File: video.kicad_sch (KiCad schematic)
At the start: 1 part

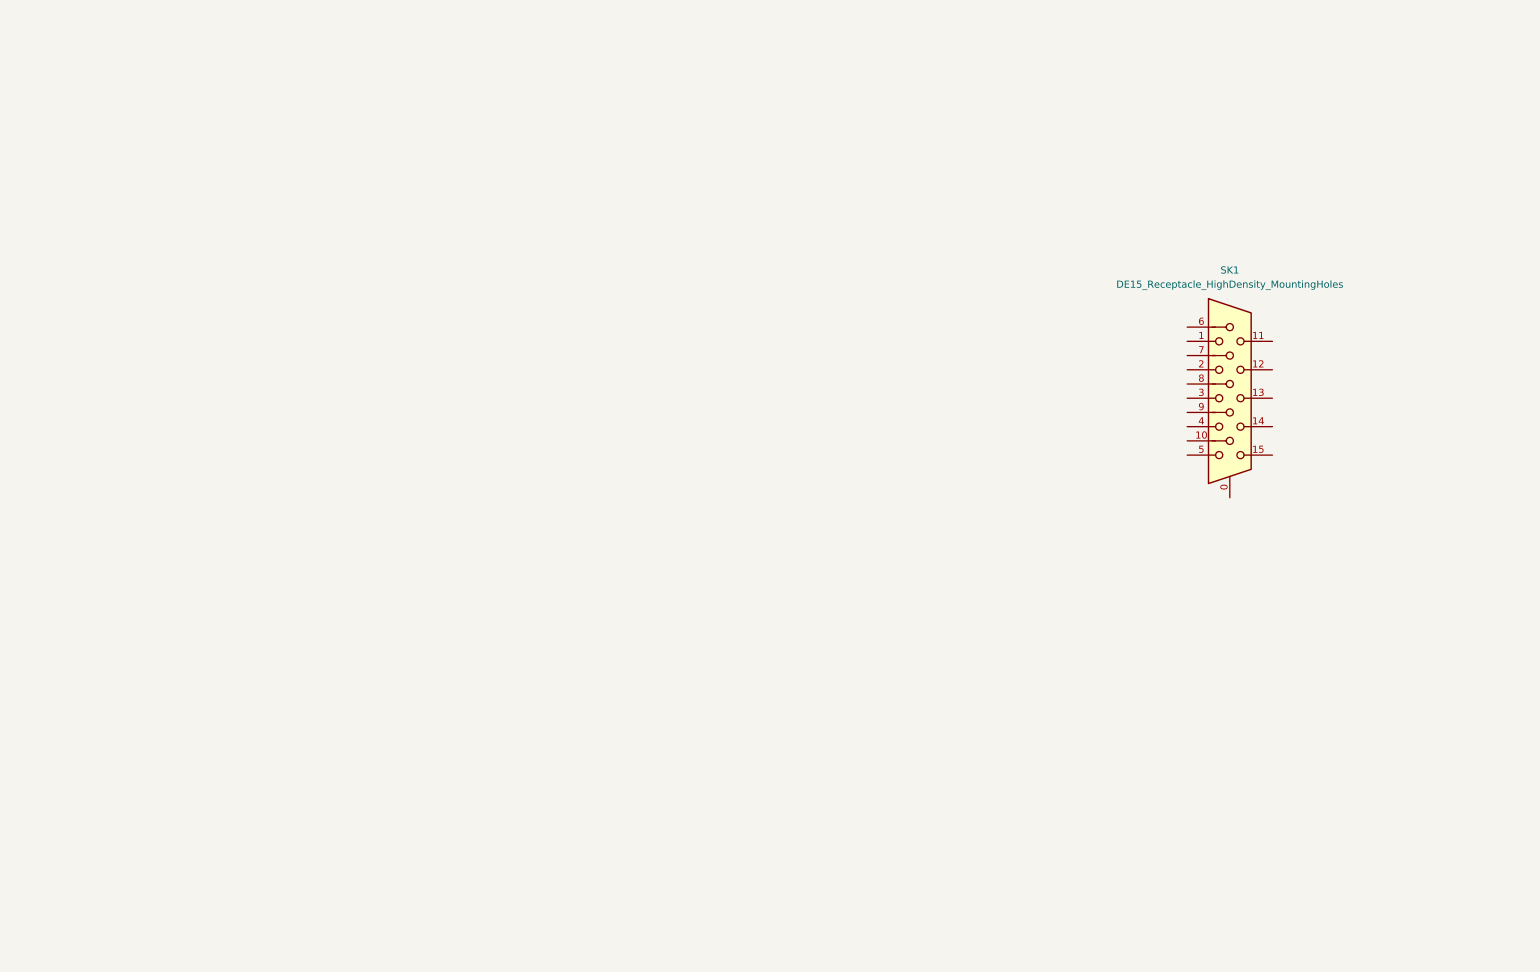
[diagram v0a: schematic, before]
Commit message: add digital video schematic
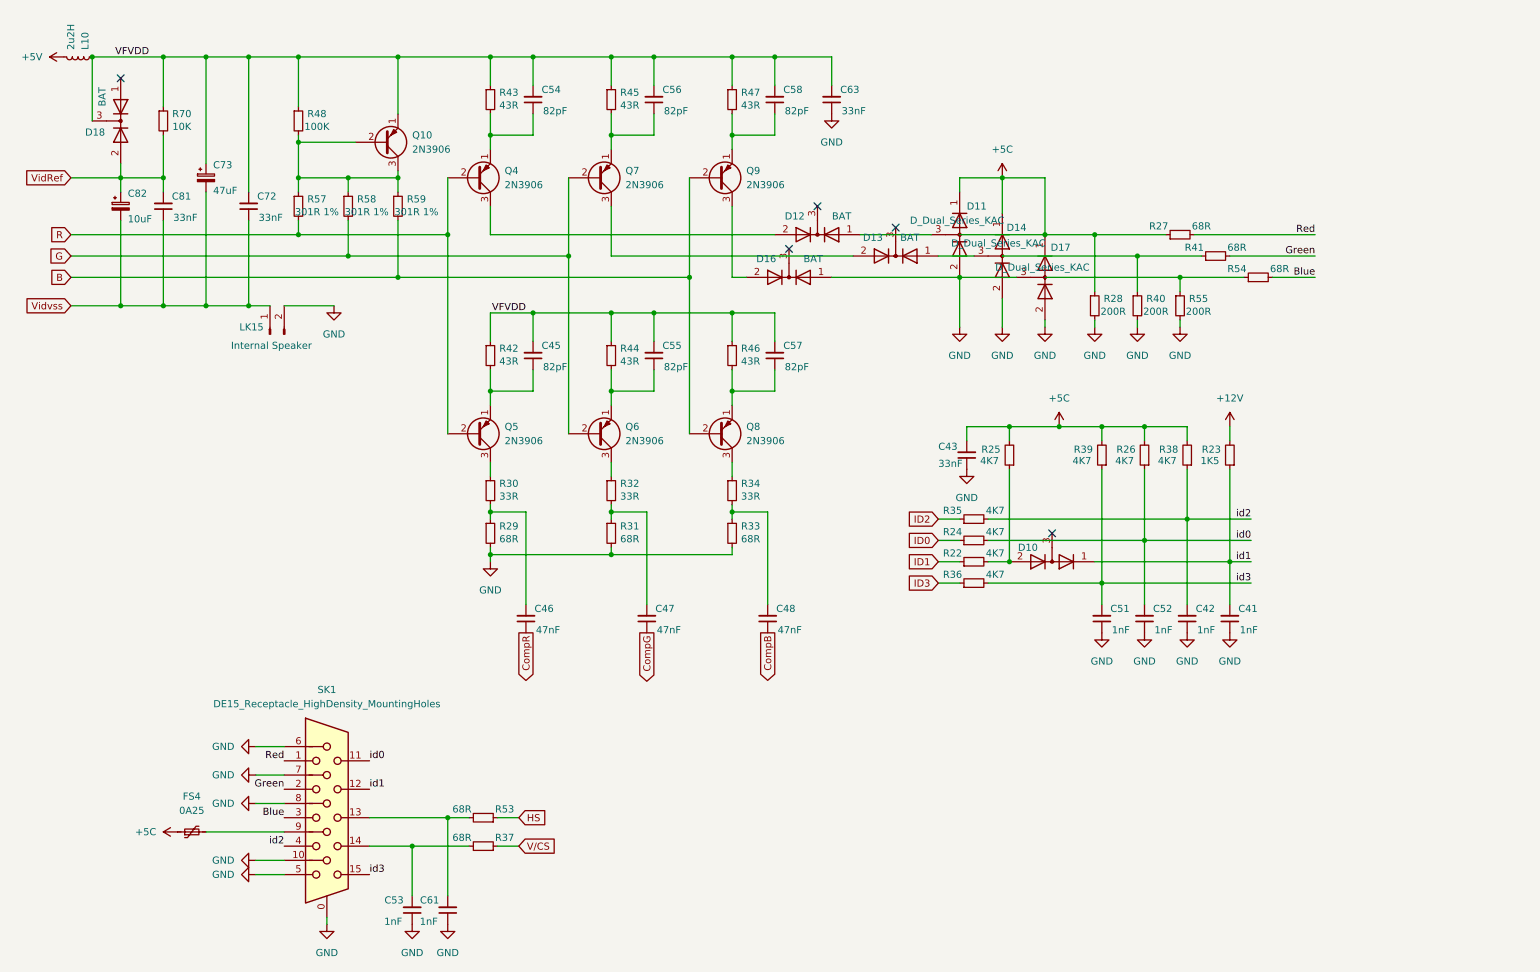
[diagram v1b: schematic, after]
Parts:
- added C41, C42, C51, C52, C53, C61: 1nF, Capacitor_SMD:C_0805_2012Metric, symbol Device:C_Small
- added C43, C63, C72, C81: 33nF, Capacitor_SMD:C_0805_2012Metric, symbol Device:C_Small
- added C45, C54, C55, C56, C57, C58: 82pF, Capacitor_SMD:C_0805_2012Metric, symbol Device:C_Small
- added C46, C47, C48: 47nF, Capacitor_SMD:C_0805_2012Metric, symbol Device:C_Small
- added C73: 47uF, Capacitor_THT:CP_Radial_Tantal_D9.0mm_P5.00mm, symbol Device:C_Polarized_Small
- added C82: 10uF, Capacitor_THT:CP_Radial_Tantal_D9.0mm_P5.00mm, symbol Device:C_Polarized_Small
- added D10: ~, Package_TO_SOT_SMD:SOT-23-3, symbol Device:D_Dual_Series_KAC
- added D11, D14, D17: D_Dual_Series_KAC, Package_TO_SOT_SMD:SOT-23-3, symbol Device:D_Dual_Series_KAC
- added D12, D13, D16, D18: BAT, Package_TO_SOT_SMD:SOT-23-3, symbol Device:D_Dual_CommonCathode_AAK
- added FS4: 0A25, Fuse:Fuse_1206_3216Metric, symbol Device:Polyfuse_Small
- added L10: 2u2H, Acorn:L_Acorn_8x3mm, symbol Device:L_Small
- added LK15: Internal Speaker, Connector_PinHeader_2.54mm:PinHeader_1x02_P2.54mm_Vertical, symbol Connector:Conn_01x02_Pin
- added Q10, Q4, Q5, Q6, Q7, Q8, Q9: 2N3906, Package_TO_SOT_SMD:SOT-23-3, symbol Transistor_BJT:2N3906
- added R22, R24, R25, R26, R35, R36, R38, R39: 4K7, Resistor_SMD:R_0805_2012Metric, symbol Device:R_Small
- added R23: 1K5, Resistor_SMD:R_0805_2012Metric, symbol Device:R_Small
- added R27, R29, R31, R33, R37, R41, R53, R54: 68R, Resistor_SMD:R_0805_2012Metric, symbol Device:R_Small
- added R28, R40, R55: 200R, Resistor_SMD:R_0805_2012Metric, symbol Device:R_Small
- added R30, R32, R34: 33R, Resistor_SMD:R_0805_2012Metric, symbol Device:R_Small
- added R42, R43, R44, R45, R46, R47: 43R, Resistor_SMD:R_0805_2012Metric, symbol Device:R_Small
- added R48: 100K, Resistor_SMD:R_0805_2012Metric, symbol Device:R_Small
- added R57, R58, R59: 301R 1%, Resistor_SMD:R_0805_2012Metric, symbol Device:R_Small
- added R70: 10K, Resistor_SMD:R_0805_2012Metric, symbol Device:R_Small
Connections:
- net GND: now reaches SK1.0
- net GND: now also SK1.10, SK1.5, SK1.6, SK1.7, SK1.8, C41.1, C42.1, C43.1, C51.1, C52.1, C53.1, C61.1, C63.1, D11.2 (A), D14.2 (A), D16.1 (A), D17.2 (A), D17.3 (common), LK15.2 (Pin_2), R28.2, R29.2, R31.2, R33.2, R40.2, R55.2
- net Red: now reaches SK1.1
- net Red: now also R27.2
- net id0: now reaches SK1.11
- net id0: now also C52.2, R24.2, R26.1
- net id1: now reaches SK1.12
- net id1: now also C41.2, D10.1 (K), R23.1
- net at SK1.13: now also C61.2, R53.2
- net at SK1.14: now also C53.2, R37.2
- net id3: now reaches SK1.15
- net id3: now also C51.2, R36.2, R39.1
- net Green: now reaches SK1.2
- net Green: now also R41.2
- net Blue: now reaches SK1.3
- net Blue: now also R54.2
- net id2: now reaches SK1.4
- net id2: now also C42.2, R35.2, R38.1
- net at SK1.9: now also FS4.2
- new net: R54.1, R55.1
- new net: C47.2, R31.1, R32.2
- new net: D10.2 (A), R22.2, R25.1
- new net: C45.1, Q5.1 (E), R42.2
- new net: D11.3 (common), D12.1 (A)
- new net: D12.2 (A), Q4.3 (C)
- new net: C54.1, Q4.1 (E), R43.2
- new net: D13.1 (A), D14.3 (common)
- new net: D13.2 (A), Q7.3 (C)
- new net: C48.2, R33.1, R34.2
- new net: C46.2, R29.1, R30.2
- new net: C56.1, Q7.1 (E), R45.2
- new net: Q5.3 (C), R30.1
- new net: C58.1, Q9.1 (E), R47.2
- new net: Q10.2 (B), Q10.3 (C), R48.2, R57.1, R58.1, R59.1
- new net: C57.1, Q8.1 (E), R46.2
- new net: C55.1, Q6.1 (E), R44.2
- new net: Q6.3 (C), R32.1
- new net: Q8.3 (C), R34.1
- new net: D16.2 (A), Q9.3 (C)
- new net: R40.1, R41.1
- new net +12V: R23.2
- new net +5C: C43.2, D11.1 (K), D14.1 (K), D17.1 (K), FS4.1, R25.2, R26.2, R27.1, R28.1, R38.2, R39.2
- new net +5V: L10.2
- new net B: Q8.2 (B), Q9.2 (B), R59.2
- new net CompB: C48.1
- new net CompG: C47.1
- new net CompR: C46.1
- new net G: Q6.2 (B), Q7.2 (B), R58.2
- new net HS: R53.1
- new net ID0: R24.1
- new net ID1: R22.1
- new net ID2: R35.1
- new net ID3: R36.1
- new net R: Q4.2 (B), Q5.2 (B), R57.2
- new net VFVDD: C45.2, C54.2, C55.2, C56.2, C57.2, C58.2, C63.2, C72.2, C73.1, D18.3 (K), L10.1, Q10.1 (E), R42.1, R43.1, R44.1, R45.1, R46.1, R47.1, R48.1, R70.1
- new net VidRef: C81.2, C82.1, D18.2 (A), R70.2
- new net Vidvss: C72.1, C73.2, C81.1, C82.2, LK15.1 (Pin_1)
- new net V/CS: R37.1
- no-connect marks 0 -> 5
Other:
- moved on the sheet: SK1

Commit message: add rf video output
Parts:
- L10: footprint Acorn:L_Acorn_8x3mm -> Inductor_THT:L_Axial_L6.6mm_D2.7mm_P10.16mm_Horizontal_Vishay_IM-2
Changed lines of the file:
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@@
 			)
 		)
-		(property "Footprint" "Acorn:L_Acorn_8x3mm"
+		(property "Footprint" "Inductor_THT:L_Axial_L6.6mm_D2.7mm_P10.16mm_Horizontal_Vishay_IM-2"
 			(at 24.13 19.05 0)
 			(effects

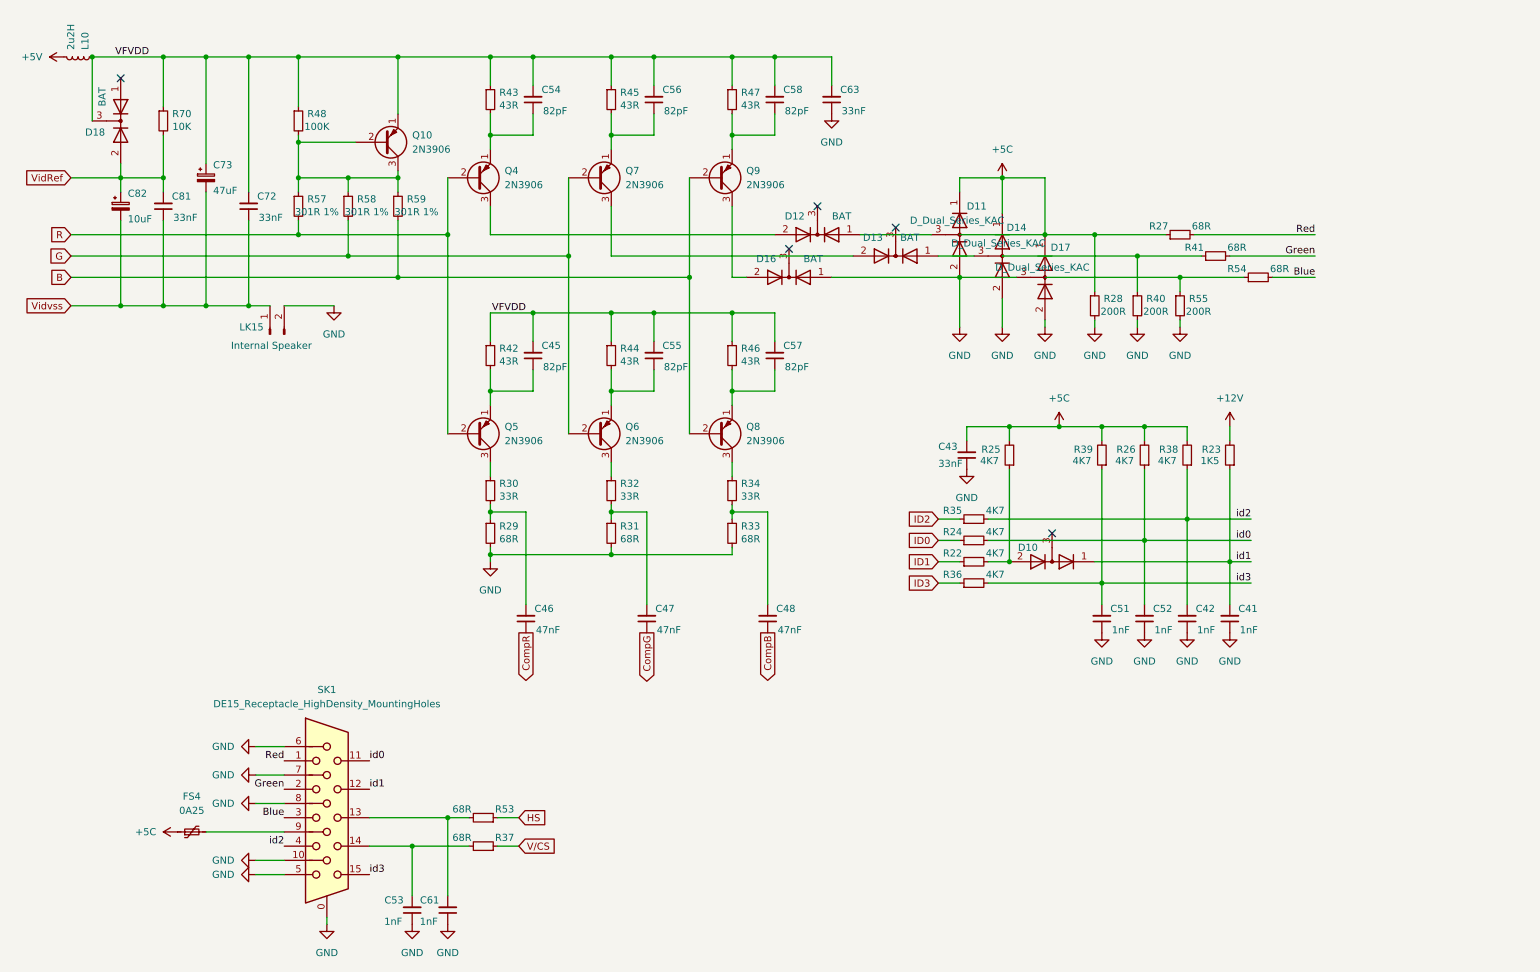
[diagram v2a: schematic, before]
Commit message: implement video routing
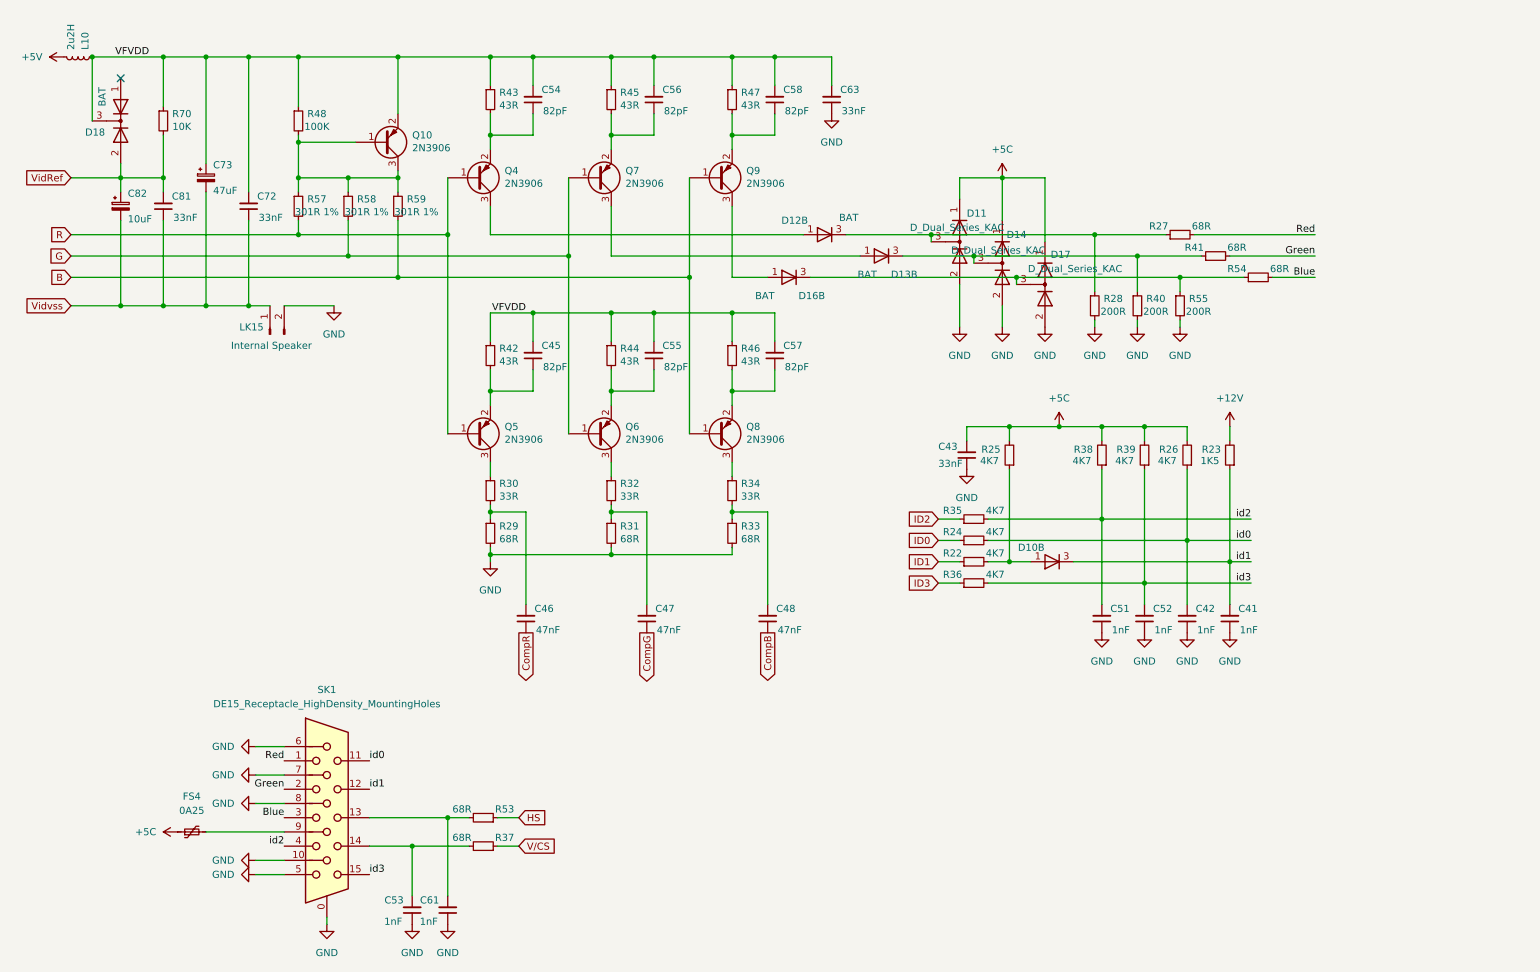
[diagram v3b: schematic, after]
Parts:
- removed Q10, Q4, Q5, Q6, Q7, Q8, Q9: 2N3906, Package_TO_SOT_SMD:SOT-23-3, symbol Transistor_BJT:2N3906
- added Q10, Q4, Q5, Q6, Q7, Q8, Q9: 2N3906, Package_TO_SOT_SMD:SOT-23-3, symbol Device:Q_PNP_BEC
- D10: symbol Device:D_Dual_Series_KAC -> Device:D_Dual_CommonAnode_AKK_Split
- D12, D13, D16: symbol Device:D_Dual_CommonCathode_AAK -> Device:D_Dual_CommonAnode_AKK_Split
- FS4: footprint Fuse:Fuse_1206_3216Metric -> Fuse:Fuse_2512_6332Metric
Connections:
- net +5C: no longer R27.1, R28.1
- net B: now also Q8.1 (B), Q9.1 (B)
- net G: now also Q6.1 (B), Q7.1 (B)
- net GND: no longer D16.1 (A), D17.3 (common)
- net R: now also Q4.1 (B), Q5.1 (B)
- net VFVDD: now also Q10.2 (E)
- net id0: now also C42.2; no longer C52.2
- net id1: now also D10.3 (K); no longer D10.1 (K)
- net id2: now also C51.2; no longer C42.2
- net id3: now also C52.2; no longer C51.2
- net at R54.1, R55.1: now also D16.3 (K), D17.3 (common)
- net at R22.2, R25.1: now also D10.1 (A); no longer D10.2 (A)
- net at C45.1, R42.2: now also Q5.2 (E)
- net at D12.1 (A): now also Q4.3 (C); no longer D11.3 (common)
- net at D12.3 (K): now also D11.3 (common), R27.1, R28.1
- net at C54.1, R43.2: now also Q4.2 (E)
- net at D13.1 (A): now also Q7.3 (C); no longer D14.3 (common)
- net at D13.3 (K): now also D14.3 (common), R40.1, R41.1
- net at C56.1, R45.2: now also Q7.2 (E)
- net at R30.1: now also Q5.3 (C)
- net at C58.1, R47.2: now also Q9.2 (E)
- net at R48.2, R57.1, R58.1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: now also Q10.1 (B), Q10.3 (C)
- net at C57.1, R46.2: now also Q8.2 (E)
- net at C55.1, R44.2: now also Q6.2 (E)
- net at R32.1: now also Q6.3 (C)
- net at R34.1: now also Q8.3 (C)
- new net: D16.1 (A), Q9.3 (C)
- no-connect marks 5 -> 1
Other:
- moved on the sheet: D11, D14, D17, R26, R38, R39

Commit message: video and keyboard routing
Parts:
- added unit 1 of D10
- added unit 1 of D12
- added unit 1 of D13
- added unit 1 of D16
- C82: footprint Capacitor_THT:CP_Radial_Tantal_D9.0mm_P5.00mm -> Capacitor_THT:CP_Radial_Tantal_D4.5mm_P5.00mm
- D10: value ~ -> BAT
- D11, D14, D17: symbol Device:D_Dual_Series_KAC -> Device:D_Dual_Series_AKC
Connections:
- net +5C: now also D11.2 (K), D14.2 (K), D17.2 (K); no longer D11.1 (K), D14.1 (K), D17.1 (K)
- net GND: now also D11.1 (A), D14.1 (A), D17.1 (A); no longer D11.2 (A), D14.2 (A), D17.2 (A)
- net VidRef: now also D18.1 (A); no longer D18.2 (A)
- no-connect marks 1 -> 5
